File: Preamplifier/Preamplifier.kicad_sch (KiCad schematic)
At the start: 90 parts, among them J10 RCA in -, J12 RCA out +, J13 RCA out -, J4 Conn_01x03_Pin, J5 RCA in +, J6 RCA in -, J7 RCA out +, J8 RCA out -, J9 RCA in +, U3 OPA1612AxD, U4 OPA1612AxD, U5 OPA1612AxD, U6 OPA1612AxD, U8 OPA1612AxD

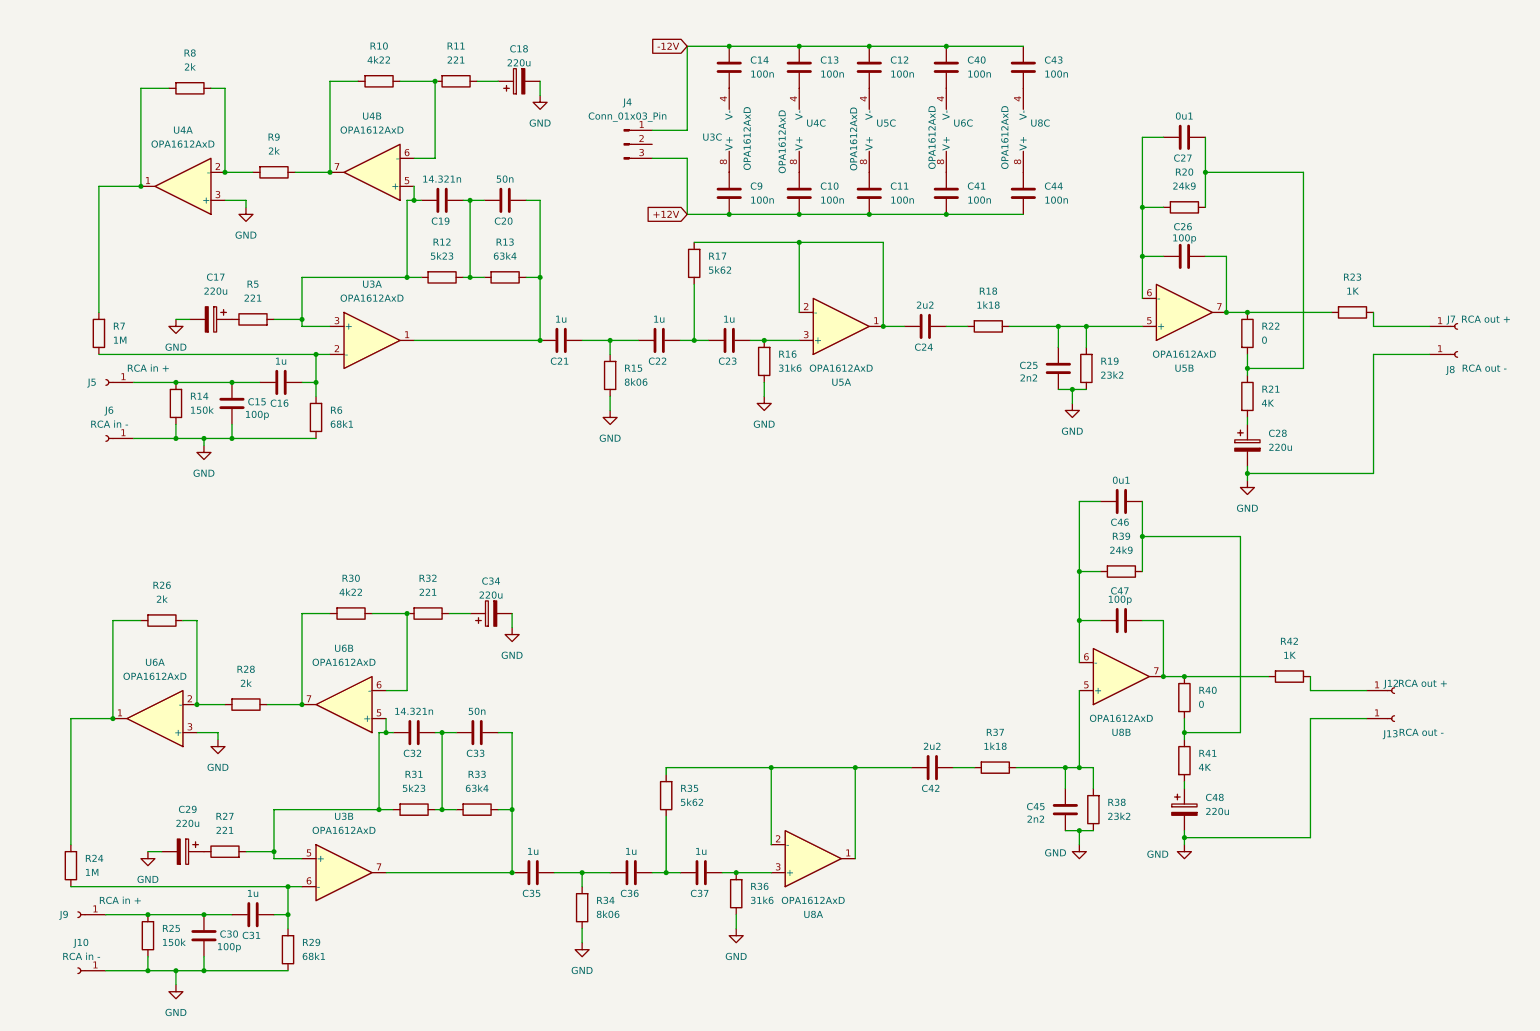
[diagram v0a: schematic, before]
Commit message: Project Structure
Updated the project structure.
Added a preamplifier project.
Added a power supply project.
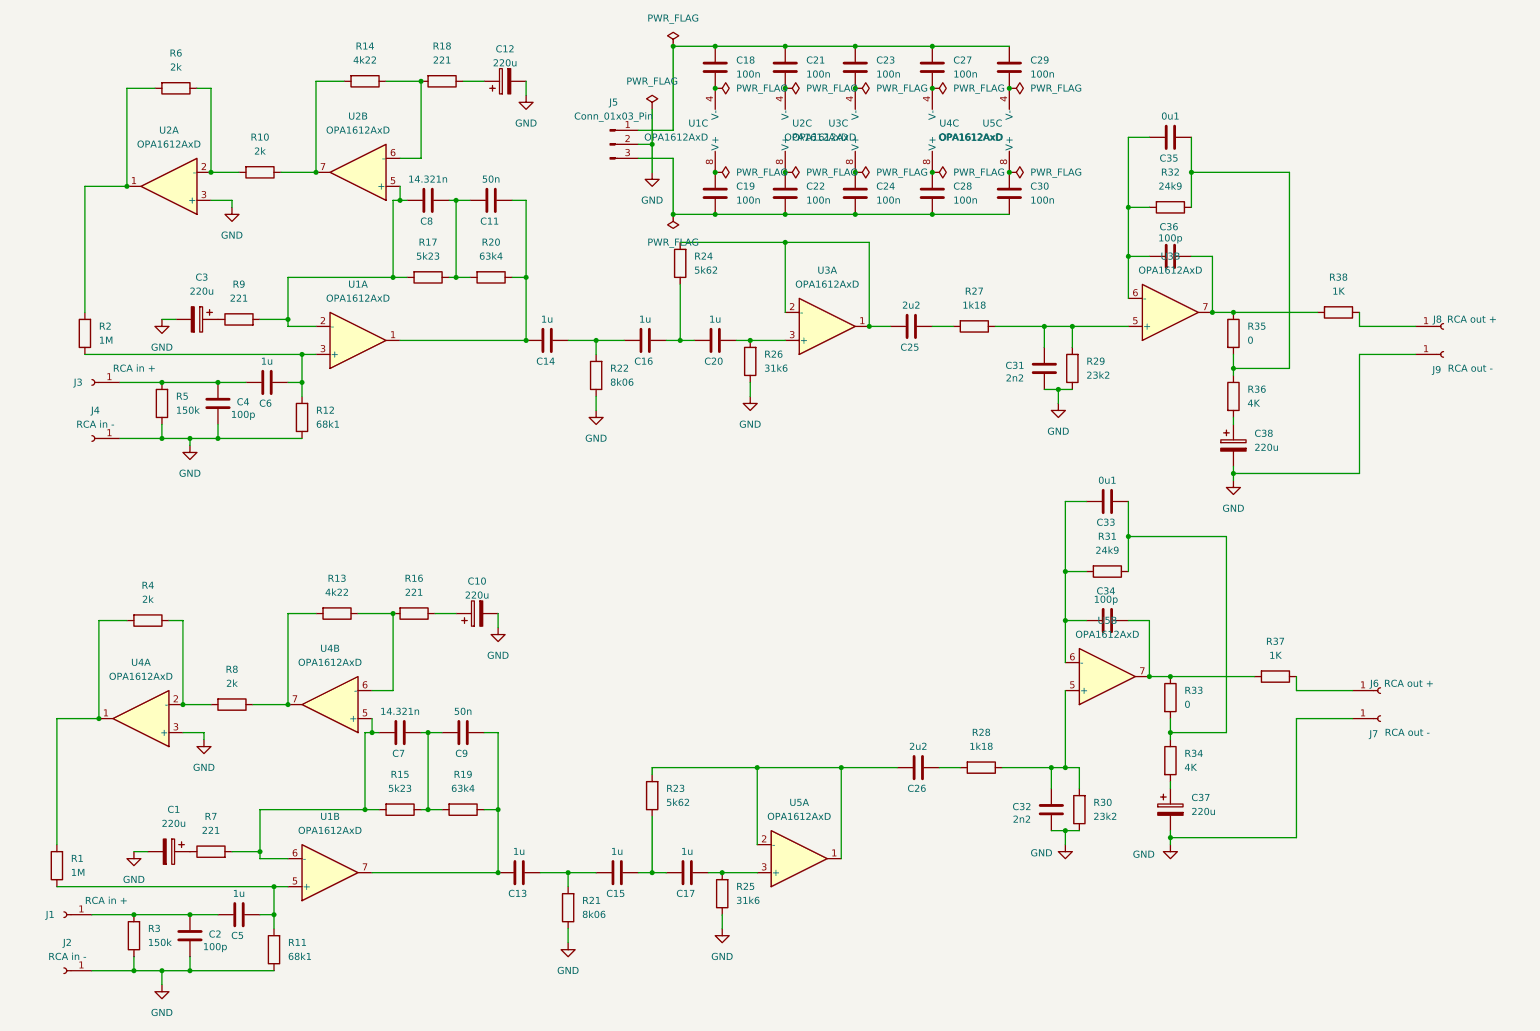
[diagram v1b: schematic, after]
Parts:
- removed C14: 100n, Capacitor_SMD:C_0805_2012Metric_Pad1.18x1.45mm_HandSolder, symbol Device:C
- removed U6, U8: OPA1612AxD, Package_SO:SOIC-8_3.9x4.9mm_P1.27mm, symbol Amplifier_Operational:OPA1612AxD
- added C18: 100n, Capacitor_SMD:C_0805_2012Metric_Pad1.18x1.45mm_HandSolder, symbol Device:C
- added U1, U2: OPA1612AxD, symbol Amplifier_Operational:OPA1612AxD
- U3, U4, U5: footprint Package_SO:SOIC-8_3.9x4.9mm_P1.27mm -> (none)
- renumbered C29 to C1, C34 to C10, C20 to C11, C18 to C12, C35 to C13, C21 to C14, C36 to C15, C22 to C16, C37 to C17, C9 to C19, C30 to C2, C23 to C20, C13 to C21, C10 to C22, C12 to C23, C11 to C24, C24 to C25, C42 to C26, C40 to C27, C41 to C28, C43 to C29, C17 to C3, C44 to C30, C25 to C31, C45 to C32, C46 to C33, C47 to C34, C27 to C35, C26 to C36, C48 to C37, C28 to C38, C15 to C4, C31 to C5, C16 to C6, C32 to C7, C19 to C8, C33 to C9, J9 to J1, J10 to J2, J5 to J3, J6 to J4, J4 to J5, J12 to J6, J13 to J7, J7 to J8, J8 to J9, R24 to R1, R9 to R10, R29 to R11, R6 to R12, R30 to R13, R10 to R14, R31 to R15, R32 to R16, R12 to R17, R11 to R18, R33 to R19, R7 to R2, R13 to R20, R34 to R21, R15 to R22, R35 to R23, R17 to R24, R36 to R25, R16 to R26, R18 to R27, R37 to R28, R19 to R29, R25 to R3, R38 to R30, R39 to R31, R20 to R32, R40 to R33, R41 to R34, R22 to R35, R21 to R36, R42 to R37, R23 to R38, R26 to R4, R14 to R5, R8 to R6, R27 to R7, R28 to R8, R5 to R9
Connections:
- net GND: now also J5.2 (Pin_2), U2.3 (+)
- net at R13.2, R8.1: now also U4.7
- net at R4.1, R8.2: now also U4.2 (-)
- net at C8.1, R17.2, R9.2: now also U1.2 (-), U2.5 (+); no longer U3.3 (+), U4.5 (+)
- net at C7.1, R15.2, R7.2: now also U4.5 (+), U1.6 (-); no longer U3.5 (+)
- net at C31.1, R27.1, R29.2: now also U3.5 (+); no longer U5.5 (+)
- net at R1.2, R4.2: now also U4.1
- net at R13.1, R16.2: now also U4.6 (-)
- net at C29.2: now also U5.4 (V-)
- net at C30.1: now also U5.8 (V+)
- net at C33.1, C34.1, R31.2: now also U5.6 (-)
- net at C25.1, R24.2: now also U3.1, U3.2 (-); no longer U5.1, U5.2 (-)
- net at C35.1, C36.1, R32.2: now also U3.6 (-); no longer U5.6 (-)
- net at C36.2, R35.1, R38.2: now also U3.7; no longer U5.7
- net at C26.1, R23.2: now also U5.1, U5.2 (-)
- net at C27.2: now also U4.4 (V-)
- net at C28.1: now also U4.8 (V+)
- net at C17.2, R25.2: now also U5.3 (+)
- net at C13.1, C9.2, R19.1: now also U1.7; no longer U3.7
- net at C20.2, R26.2: now also U3.3 (+); no longer U5.3 (+)
- net at R10.1, R14.2: now also U2.7; no longer U4.7
- net at R10.2, R6.1: now also U2.2 (-); no longer U4.2 (-)
- net at C23.2: now also U3.4 (V-); no longer U5.4 (V-)
- net at R14.1, R18.2: now also U2.6 (-); no longer U4.6 (-)
- net at C5.2, R1.1, R11.2: now also U1.5 (+); no longer U3.6 (-)
- net at C24.1: now also U3.8 (V+); no longer U5.8 (V+)
- net at C21.2: now also U2.4 (V-); no longer U4.4 (V-)
- net at C32.1, R28.1, R30.2: now also U5.5 (+)
- net at C11.2, C14.1, R20.1: now also U1.1; no longer U3.1
- net at C34.2, R33.1, R37.2: now also U5.7
- net at R2.2, R6.2: now also U2.1; no longer U4.1
- net at C19.1: now also U1.8 (V+); no longer U3.8 (V+)
- net at C22.1: now also U2.8 (V+); no longer U4.8 (V+)
- net at C6.2, R12.2, R2.1: now also U1.3 (+); no longer U3.2 (-)
- net +12V: no longer names the net of C19.2, C22.2, C24.2, C28.2, C30.2, J5.3 (Pin_3)
- net -12V: no longer names the net of C21.1, C23.1, C27.1, C29.1, J5.1 (Pin_1)
- net -12V: now also C18.1
- new net: C18.2, U1.4 (V-)
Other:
- moved on the sheet: C1, C10, C11, C12, C13, C14, C15, C16, C17, C19, C2, C20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

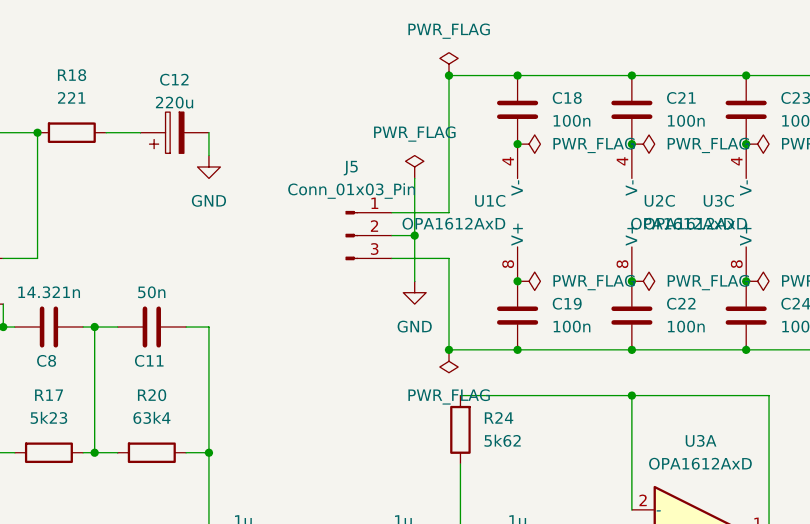
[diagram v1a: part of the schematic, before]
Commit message: Preamplifier Board
Added the preamplifier board design.
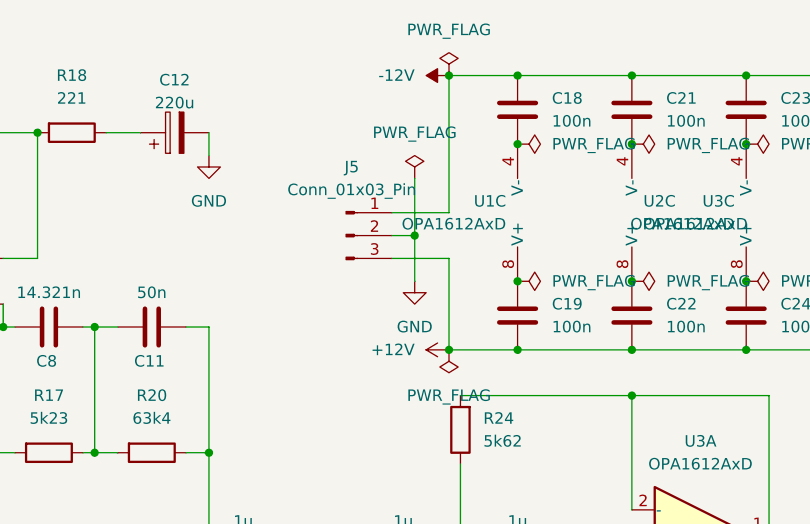
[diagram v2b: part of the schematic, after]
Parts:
- U1, U2, U3, U4, U5: footprint (none) -> Package_SO:SOIC-8_3.9x4.9mm_P1.27mm
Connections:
- net -12V: now reaches C18.1, C21.1, C23.1, C27.1, C29.1, J5.1 (Pin_1)
- net +12V: now reaches C19.2, C22.2, C24.2, C28.2, C30.2, J5.3 (Pin_3)

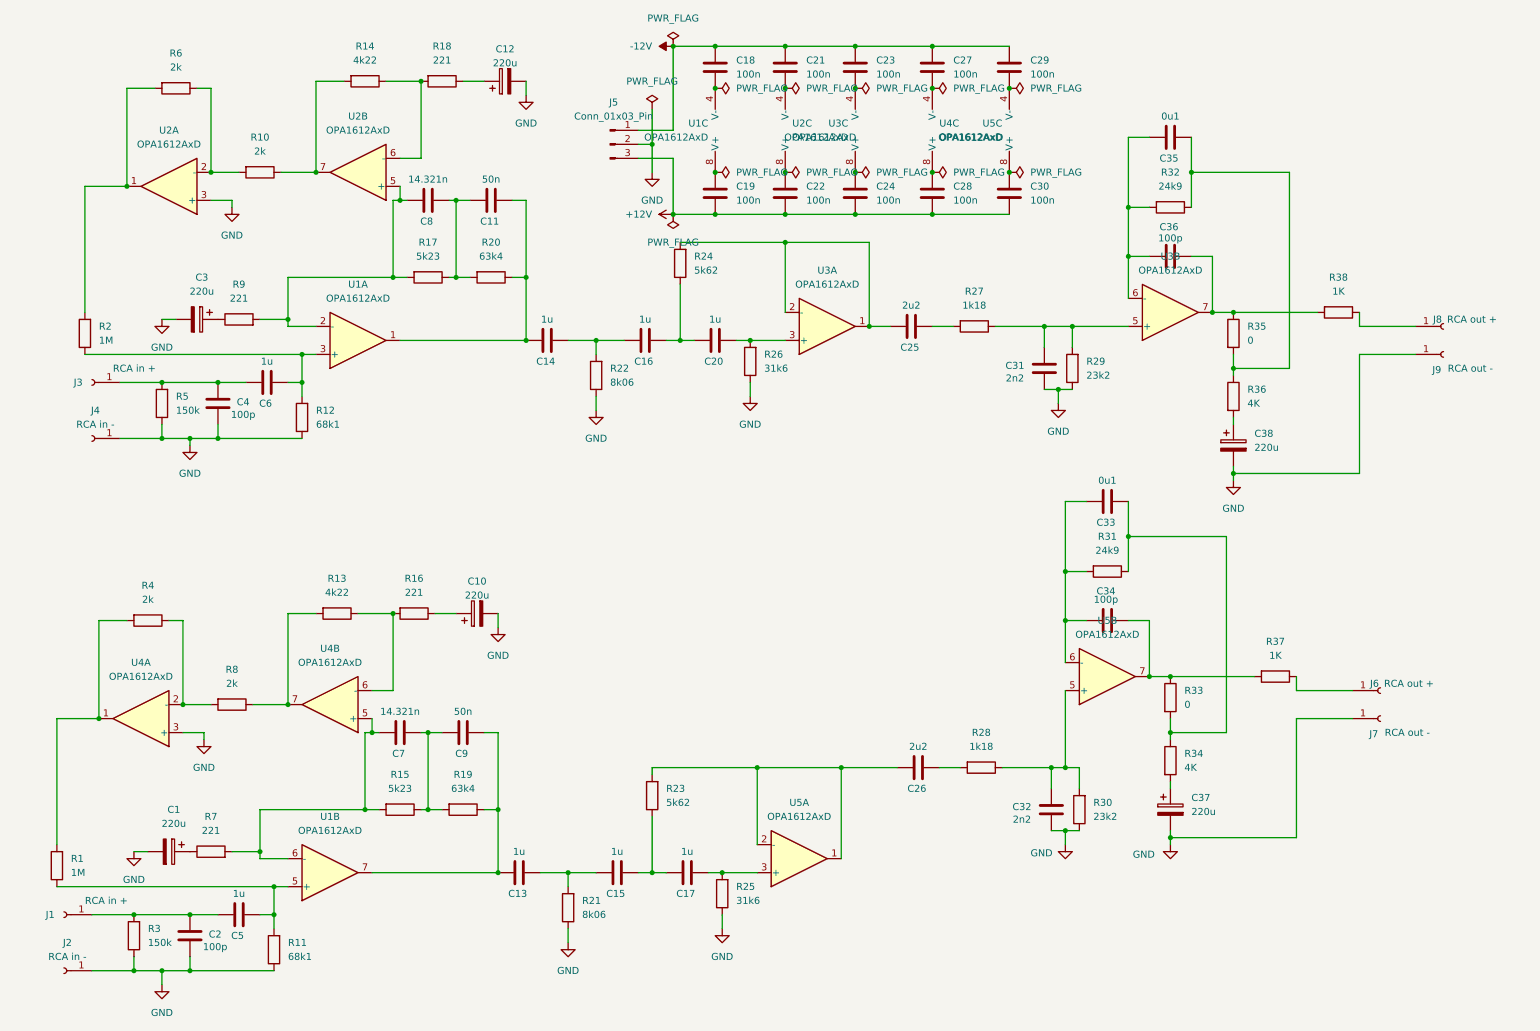
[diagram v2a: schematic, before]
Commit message: Initial Production
Set the production configuration.
Updated the preamplifier board design.
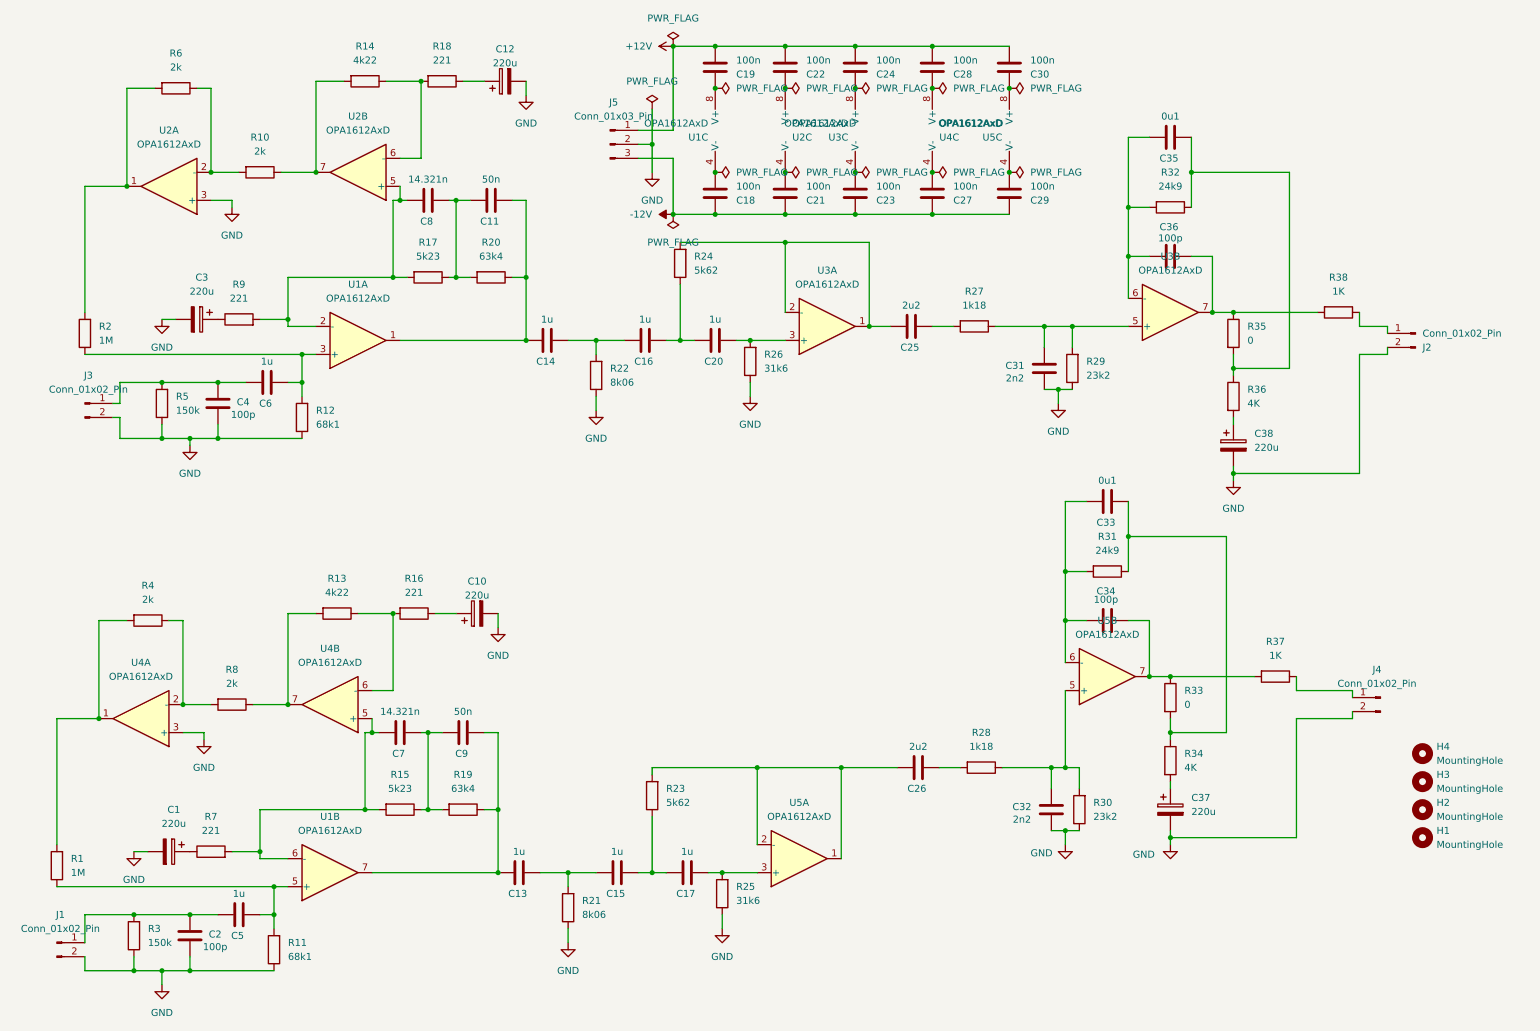
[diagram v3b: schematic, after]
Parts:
- removed J1, J3: RCA in +, Connector_Wire:SolderWire-0.5sqmm_1x01_D0.9mm_OD2.1mm, symbol Connector:Conn_01x01_Socket
- removed J2, J4: RCA in -, Connector_Wire:SolderWire-0.5sqmm_1x01_D0.9mm_OD2.1mm, symbol Connector:Conn_01x01_Socket
- removed J6, J8: RCA out +, Connector_Wire:SolderWire-0.5sqmm_1x01_D0.9mm_OD2.1mm, symbol Connector:Conn_01x01_Socket
- removed J7, J9: RCA out -, Connector_Wire:SolderWire-0.5sqmm_1x01_D0.9mm_OD2.1mm, symbol Connector:Conn_01x01_Socket
- added H1, H2, H3, H4: MountingHole, MountingHole:MountingHole_3.2mm_M3, symbol Mechanical:MountingHole
- added J1, J2, J3, J4: Conn_01x02_Pin, Connector_Molex:Molex_KK-254_AE-6410-02A_1x02_P2.54mm_Vertical, symbol Connector:Conn_01x02_Pin
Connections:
- net +12V: now also J5.1 (Pin_1); no longer J5.3 (Pin_3)
- net -12V: now also J5.3 (Pin_3); no longer J5.1 (Pin_1)
- net GND: now also J1.2 (Pin_2), J2.2 (Pin_2), J3.2 (Pin_2), J4.2 (Pin_2)
- net at R37.1: now also J4.1 (Pin_1)
- net at C2.1, C5.1, R3.2: now also J1.1 (Pin_1)
- net at R38.1: now also J2.1 (Pin_1)
- net at C4.1, C6.1, R5.2: now also J3.1 (Pin_1)
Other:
- moved on the sheet: C18, C19, C21, C22, C23, C24, C27, C28, C29, C30, U2C, U4C

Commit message: Production Ready REAL Ready
Changed C47n to 1206
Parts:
- C11, C9: value 50n -> 47n; footprint Capacitor_SMD:C_0805_2012Metric_Pad1.18x1.45mm_HandSolder -> Capacitor_SMD:C_1206_3216Metric_Pad1.33x1.80mm_HandSolder
- C7, C8: value 14.321n -> 13n
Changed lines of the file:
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@@
 			)
 		)
-		(property "Value" "14.321n"
+		(property "Value" "13n"
 			(at 81.28 137.16 90)
 			(effects
@@
 			)
 		)
-		(property "Value" "50n"
+		(property "Value" "47n"
 			(at 97.79 40.64 90)
 			(effects
@@
 			)
 		)
-		(property "Footprint" "Capacitor_SMD:C_0805_2012Metric_Pad1.18x1.45mm_HandSolder"
+		(property "Footprint" "Capacitor_SMD:C_1206_3216Metric_Pad1.33x1.80mm_HandSolder"
 			(at 101.6 43.4848 0)
 			(effects
@@
 			)
 		)
-		(property "Value" "14.321n"
+		(property "Value" "13n"
 			(at 86.36 40.64 90)
 			(effects
@@
 			)
 		)
-		(property "Value" "50n"
+		(property "Value" "47n"
 			(at 92.71 137.16 90)
 			(effects
@@
 			)
 		)
-		(property "Footprint" "Capacitor_SMD:C_0805_2012Metric_Pad1.18x1.45mm_HandSolder"
+		(property "Footprint" "Capacitor_SMD:C_1206_3216Metric_Pad1.33x1.80mm_HandSolder"
 			(at 96.52 140.0048 0)
 			(effects
